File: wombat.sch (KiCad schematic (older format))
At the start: 188 parts, among them J1 Conn_01x01, J2 Conn_01x01, SW1 SW_SPST, SW10 SW_SPST, SW11 SW_SPST, SW12 SW_SPST, SW13 SW_SPST, SW14 SW_SPST, SW15 SW_SPST, SW16 SW_SPST, SW17 SW_SPST, SW18 SW_SPST, SW19 SW_SPST, SW2 SW_SPST, SW20 SW_SPST, SW21 SW_SPST, SW22 SW_SPST, SW23 SW_SPST, SW24 SW_SPST, SW25 SW_SPST, SW26 SW_SPST, SW27 SW_SPST, SW28 SW_SPST, SW29 SW_SPST, SW3 SW_SPST, SW30 SW_SPST, SW31 SW_SPST, SW32 SW_SPST, SW33 SW_SPST, SW34 SW_SPST, SW35 SW_SPST, SW36 SW_SPST, SW37 SW_SPST, SW38 SW_SPST, SW39 SW_SPST, SW4 SW_SPST, SW40 SW_SPST, SW41 SW_SPST, SW42 SW_SPST, SW43 SW_Push, SW44 SW_SPST, SW45 SW_SPST, SW46 SW_SPST, SW47 SW_SPST, SW5 SW_SPST, SW6 SW_SPST, SW7 SW_SPST, SW8 SW_SPST, SW9 SW_SPST, U1 ProMicro

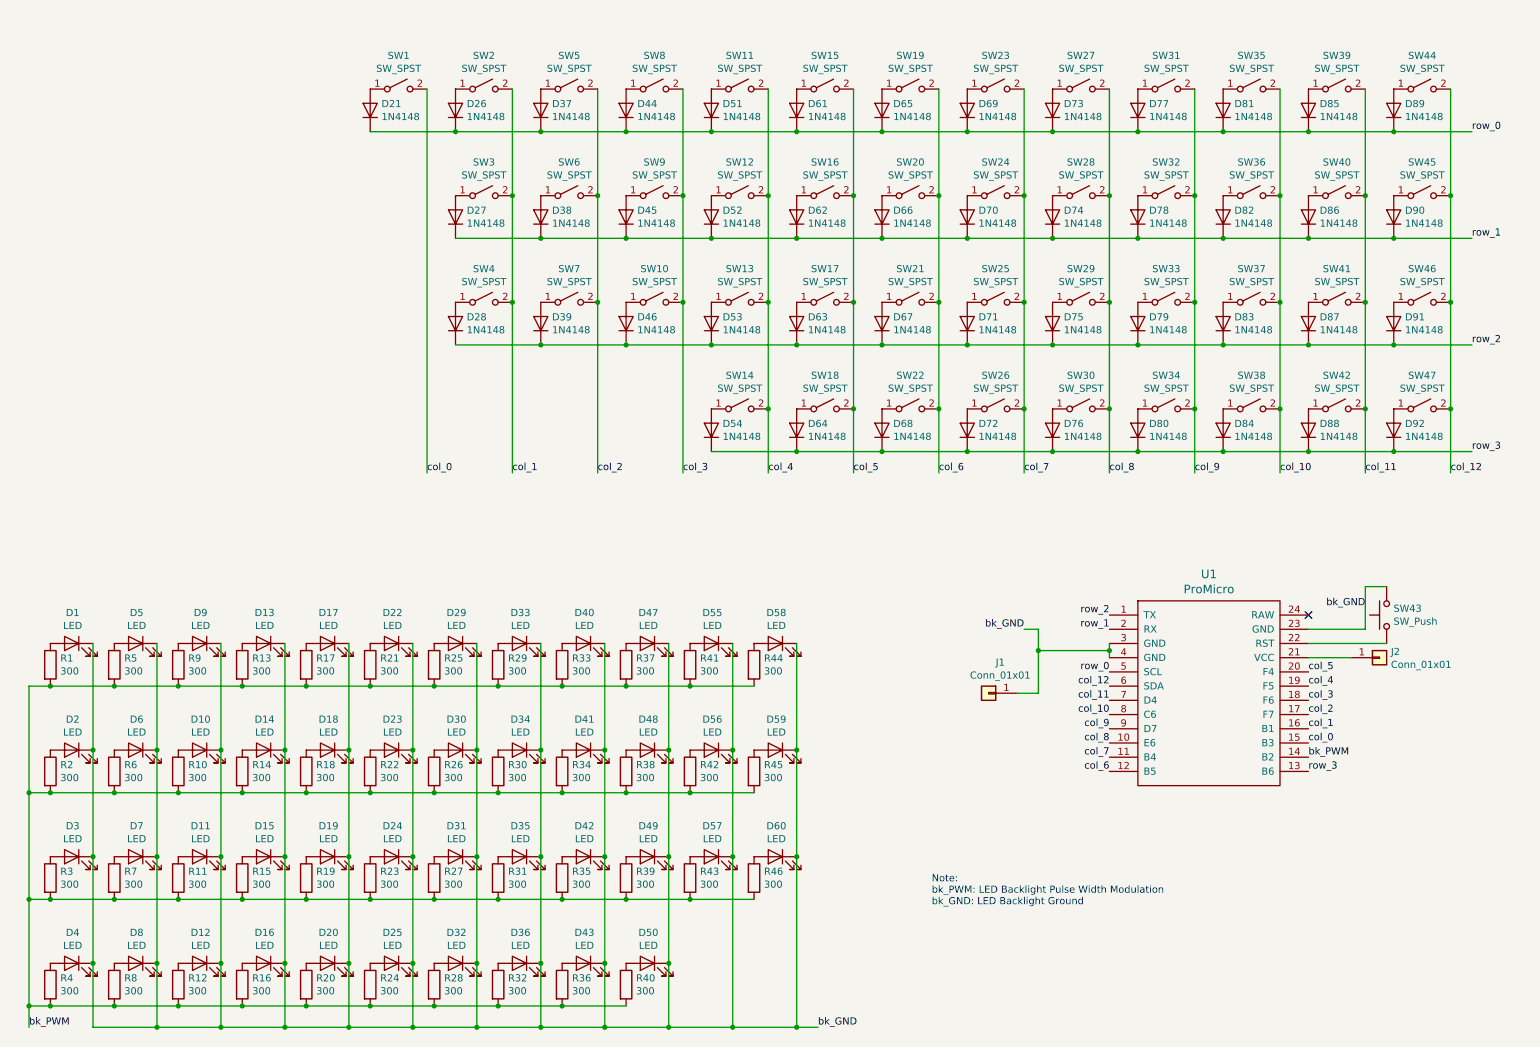
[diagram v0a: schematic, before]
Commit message: annotate components
associate symbols to footprints
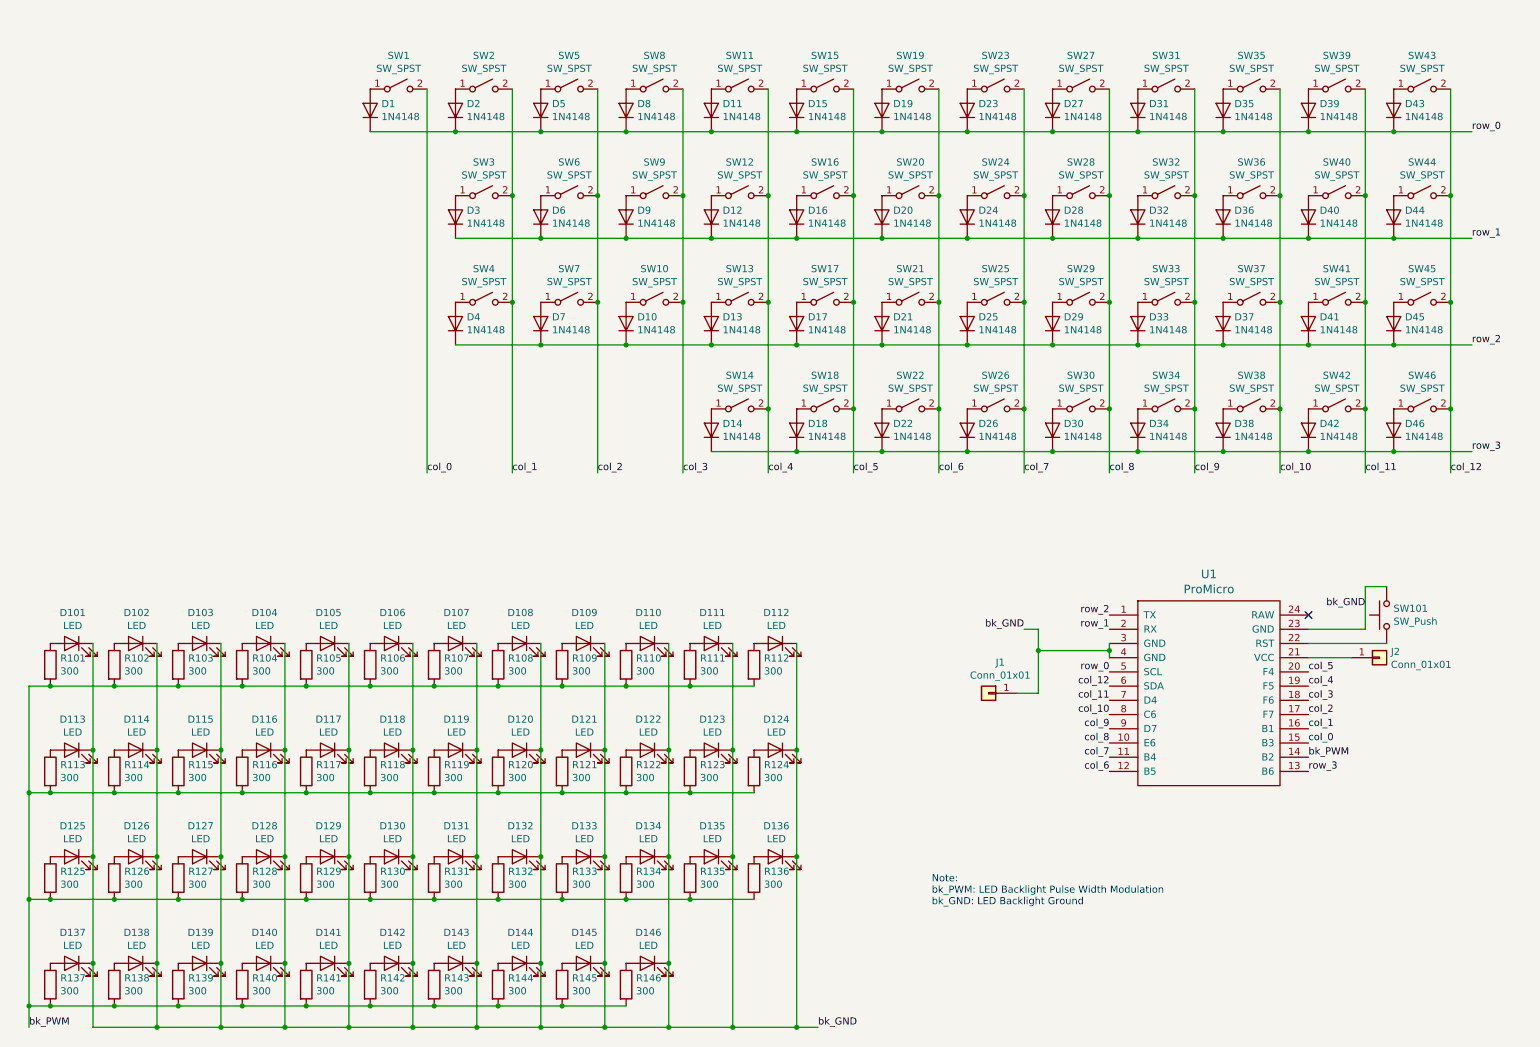
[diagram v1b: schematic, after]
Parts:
- D1: renamed from D21; footprint Diode_THT:D_DO-35_SOD27_P7.62mm_Horizontal -> Diode_SMD:D_0805_2012Metric_Pad1.15x1.40mm_HandSolder
- D10: renamed from D46; footprint Diode_THT:D_DO-35_SOD27_P7.62mm_Horizontal -> Diode_SMD:D_SOD-123
- D101: renamed from D1; footprint (none) -> LED_THT:LED_D2.0mm_W4.8mm_H2.5mm_FlatTop
- D102: renamed from D5; footprint (none) -> LED_THT:LED_D2.0mm_W4.8mm_H2.5mm_FlatTop
- D103: renamed from D9; footprint (none) -> LED_THT:LED_D2.0mm_W4.8mm_H2.5mm_FlatTop
- D104: renamed from D13; footprint (none) -> LED_THT:LED_D2.0mm_W4.8mm_H2.5mm_FlatTop
- D105: renamed from D17; footprint (none) -> LED_THT:LED_D2.0mm_W4.8mm_H2.5mm_FlatTop
- D106: renamed from D22; footprint (none) -> LED_THT:LED_D2.0mm_W4.8mm_H2.5mm_FlatTop
- D107: renamed from D29; footprint (none) -> LED_THT:LED_D2.0mm_W4.8mm_H2.5mm_FlatTop
- D108: renamed from D33; footprint (none) -> LED_THT:LED_D2.0mm_W4.8mm_H2.5mm_FlatTop
- D109: renamed from D40; footprint (none) -> LED_THT:LED_D2.0mm_W4.8mm_H2.5mm_FlatTop
- D11: renamed from D51; footprint Diode_THT:D_DO-35_SOD27_P7.62mm_Horizontal -> Diode_SMD:D_SOD-123
- D110: renamed from D47; footprint (none) -> LED_THT:LED_D2.0mm_W4.8mm_H2.5mm_FlatTop
- D111: renamed from D55; footprint (none) -> LED_THT:LED_D2.0mm_W4.8mm_H2.5mm_FlatTop
- D112: renamed from D58; footprint (none) -> LED_THT:LED_D2.0mm_W4.8mm_H2.5mm_FlatTop
- D113: renamed from D2; footprint (none) -> LED_THT:LED_D2.0mm_W4.8mm_H2.5mm_FlatTop
- D114: renamed from D6; footprint (none) -> LED_THT:LED_D2.0mm_W4.8mm_H2.5mm_FlatTop
- D115: renamed from D10; footprint (none) -> LED_THT:LED_D2.0mm_W4.8mm_H2.5mm_FlatTop
- D116: renamed from D14; footprint (none) -> LED_THT:LED_D2.0mm_W4.8mm_H2.5mm_FlatTop
- D117: renamed from D18; footprint (none) -> LED_THT:LED_D2.0mm_W4.8mm_H2.5mm_FlatTop
- D118: renamed from D23; footprint (none) -> LED_THT:LED_D2.0mm_W4.8mm_H2.5mm_FlatTop
- D119: renamed from D30; footprint (none) -> LED_THT:LED_D2.0mm_W4.8mm_H2.5mm_FlatTop
- D12: renamed from D52; footprint Diode_THT:D_DO-35_SOD27_P7.62mm_Horizontal -> Diode_SMD:D_SOD-123
- D120: renamed from D34; footprint (none) -> LED_THT:LED_D2.0mm_W4.8mm_H2.5mm_FlatTop
- D121: renamed from D41; footprint (none) -> LED_THT:LED_D2.0mm_W4.8mm_H2.5mm_FlatTop
- D122: renamed from D48; footprint (none) -> LED_THT:LED_D2.0mm_W4.8mm_H2.5mm_FlatTop
- D123: renamed from D56; footprint (none) -> LED_THT:LED_D2.0mm_W4.8mm_H2.5mm_FlatTop
- D124: renamed from D59; footprint (none) -> LED_THT:LED_D2.0mm_W4.8mm_H2.5mm_FlatTop
- D125: renamed from D3; footprint (none) -> LED_THT:LED_D2.0mm_W4.8mm_H2.5mm_FlatTop
- D126: renamed from D7; footprint (none) -> LED_THT:LED_D2.0mm_W4.8mm_H2.5mm_FlatTop
- D127: renamed from D11; footprint (none) -> LED_THT:LED_D2.0mm_W4.8mm_H2.5mm_FlatTop
- D128: renamed from D15; footprint (none) -> LED_THT:LED_D2.0mm_W4.8mm_H2.5mm_FlatTop
- D129: renamed from D19; footprint (none) -> LED_THT:LED_D2.0mm_W4.8mm_H2.5mm_FlatTop
- D13: renamed from D53; footprint Diode_THT:D_DO-35_SOD27_P7.62mm_Horizontal -> Diode_SMD:D_SOD-123
- D130: renamed from D24; footprint (none) -> LED_THT:LED_D2.0mm_W4.8mm_H2.5mm_FlatTop
- D131: renamed from D31; footprint (none) -> LED_THT:LED_D2.0mm_W4.8mm_H2.5mm_FlatTop
- D132: renamed from D35; footprint (none) -> LED_THT:LED_D2.0mm_W4.8mm_H2.5mm_FlatTop
- D133: renamed from D42; footprint (none) -> LED_THT:LED_D2.0mm_W4.8mm_H2.5mm_FlatTop
- D134: renamed from D49; footprint (none) -> LED_THT:LED_D2.0mm_W4.8mm_H2.5mm_FlatTop
- D135: renamed from D57; footprint (none) -> LED_THT:LED_D2.0mm_W4.8mm_H2.5mm_FlatTop
- D136: renamed from D60; footprint (none) -> LED_THT:LED_D2.0mm_W4.8mm_H2.5mm_FlatTop
- D137: renamed from D4; footprint (none) -> LED_THT:LED_D2.0mm_W4.8mm_H2.5mm_FlatTop
- D138: renamed from D8; footprint (none) -> LED_THT:LED_D2.0mm_W4.8mm_H2.5mm_FlatTop
- D139: renamed from D12; footprint (none) -> LED_THT:LED_D2.0mm_W4.8mm_H2.5mm_FlatTop
- D14: renamed from D54; footprint Diode_THT:D_DO-35_SOD27_P7.62mm_Horizontal -> Diode_SMD:D_SOD-123
- D140: renamed from D16; footprint (none) -> LED_THT:LED_D2.0mm_W4.8mm_H2.5mm_FlatTop
- D141: renamed from D20; footprint (none) -> LED_THT:LED_D2.0mm_W4.8mm_H2.5mm_FlatTop
- D142: renamed from D25; footprint (none) -> LED_THT:LED_D2.0mm_W4.8mm_H2.5mm_FlatTop
- D143: renamed from D32; footprint (none) -> LED_THT:LED_D2.0mm_W4.8mm_H2.5mm_FlatTop
- D144: renamed from D36; footprint (none) -> LED_THT:LED_D2.0mm_W4.8mm_H2.5mm_FlatTop
- D145: renamed from D43; footprint (none) -> LED_THT:LED_D2.0mm_W4.8mm_H2.5mm_FlatTop
- D146: renamed from D50; footprint (none) -> LED_THT:LED_D2.0mm_W4.8mm_H2.5mm_FlatTop
- D15: renamed from D61; footprint Diode_THT:D_DO-35_SOD27_P7.62mm_Horizontal -> Diode_SMD:D_SOD-123
- D16: renamed from D62; footprint Diode_THT:D_DO-35_SOD27_P7.62mm_Horizontal -> Diode_SMD:D_SOD-123
- D17: renamed from D63; footprint Diode_THT:D_DO-35_SOD27_P7.62mm_Horizontal -> Diode_SMD:D_SOD-123
- D18: renamed from D64; footprint Diode_THT:D_DO-35_SOD27_P7.62mm_Horizontal -> Diode_SMD:D_SOD-123
- D19: renamed from D65; footprint Diode_THT:D_DO-35_SOD27_P7.62mm_Horizontal -> Diode_SMD:D_SOD-123
- D2: renamed from D26; footprint Diode_THT:D_DO-35_SOD27_P7.62mm_Horizontal -> Diode_SMD:D_SOD-123
- D20: renamed from D66; footprint Diode_THT:D_DO-35_SOD27_P7.62mm_Horizontal -> Diode_SMD:D_SOD-123
- D21: renamed from D67; footprint Diode_THT:D_DO-35_SOD27_P7.62mm_Horizontal -> Diode_SMD:D_SOD-123
- D22: renamed from D68; footprint Diode_THT:D_DO-35_SOD27_P7.62mm_Horizontal -> Diode_SMD:D_SOD-123
- D23: renamed from D69; footprint Diode_THT:D_DO-35_SOD27_P7.62mm_Horizontal -> Diode_SMD:D_SOD-123
- D24: renamed from D70; footprint Diode_THT:D_DO-35_SOD27_P7.62mm_Horizontal -> Diode_SMD:D_SOD-123
- D25: renamed from D71; footprint Diode_THT:D_DO-35_SOD27_P7.62mm_Horizontal -> Diode_SMD:D_SOD-123
- D26: renamed from D72; footprint Diode_THT:D_DO-35_SOD27_P7.62mm_Horizontal -> Diode_SMD:D_SOD-123
- D27: renamed from D73; footprint Diode_THT:D_DO-35_SOD27_P7.62mm_Horizontal -> Diode_SMD:D_SOD-123
- D28: renamed from D74; footprint Diode_THT:D_DO-35_SOD27_P7.62mm_Horizontal -> Diode_SMD:D_SOD-123
- D29: renamed from D75; footprint Diode_THT:D_DO-35_SOD27_P7.62mm_Horizontal -> Diode_SMD:D_SOD-123
- D3: renamed from D27; footprint Diode_THT:D_DO-35_SOD27_P7.62mm_Horizontal -> Diode_SMD:D_SOD-123
- D30: renamed from D76; footprint Diode_THT:D_DO-35_SOD27_P7.62mm_Horizontal -> Diode_SMD:D_SOD-123
- D31: renamed from D77; footprint Diode_THT:D_DO-35_SOD27_P7.62mm_Horizontal -> Diode_SMD:D_SOD-123
- D32: renamed from D78; footprint Diode_THT:D_DO-35_SOD27_P7.62mm_Horizontal -> Diode_SMD:D_SOD-123
- D33: renamed from D79; footprint Diode_THT:D_DO-35_SOD27_P7.62mm_Horizontal -> Diode_SMD:D_SOD-123
- D34: renamed from D80; footprint Diode_THT:D_DO-35_SOD27_P7.62mm_Horizontal -> Diode_SMD:D_SOD-123
- D35: renamed from D81; footprint Diode_THT:D_DO-35_SOD27_P7.62mm_Horizontal -> Diode_SMD:D_SOD-123
- D36: renamed from D82; footprint Diode_THT:D_DO-35_SOD27_P7.62mm_Horizontal -> Diode_SMD:D_SOD-123
- D37: renamed from D83; footprint Diode_THT:D_DO-35_SOD27_P7.62mm_Horizontal -> Diode_SMD:D_SOD-123
- D38: renamed from D84; footprint Diode_THT:D_DO-35_SOD27_P7.62mm_Horizontal -> Diode_SMD:D_SOD-123
- D39: renamed from D85; footprint Diode_THT:D_DO-35_SOD27_P7.62mm_Horizontal -> Diode_SMD:D_SOD-123
- D4: renamed from D28; footprint Diode_THT:D_DO-35_SOD27_P7.62mm_Horizontal -> Diode_SMD:D_SOD-123
- D40: renamed from D86; footprint Diode_THT:D_DO-35_SOD27_P7.62mm_Horizontal -> Diode_SMD:D_SOD-123
- D41: renamed from D87; footprint Diode_THT:D_DO-35_SOD27_P7.62mm_Horizontal -> Diode_SMD:D_SOD-123
- D42: renamed from D88; footprint Diode_THT:D_DO-35_SOD27_P7.62mm_Horizontal -> Diode_SMD:D_SOD-123
- D43: renamed from D89; footprint Diode_THT:D_DO-35_SOD27_P7.62mm_Horizontal -> Diode_SMD:D_SOD-123
- D44: renamed from D90; footprint Diode_THT:D_DO-35_SOD27_P7.62mm_Horizontal -> Diode_SMD:D_SOD-123
- D45: renamed from D91; footprint Diode_THT:D_DO-35_SOD27_P7.62mm_Horizontal -> Diode_SMD:D_SOD-123
- D46: renamed from D92; footprint Diode_THT:D_DO-35_SOD27_P7.62mm_Horizontal -> Diode_SMD:D_SOD-123
- D5: renamed from D37; footprint Diode_THT:D_DO-35_SOD27_P7.62mm_Horizontal -> Diode_SMD:D_SOD-123
- D6: renamed from D38; footprint Diode_THT:D_DO-35_SOD27_P7.62mm_Horizontal -> Diode_SMD:D_SOD-123
- D7: renamed from D39; footprint Diode_THT:D_DO-35_SOD27_P7.62mm_Horizontal -> Diode_SMD:D_SOD-123
- D8: renamed from D44; footprint Diode_THT:D_DO-35_SOD27_P7.62mm_Horizontal -> Diode_SMD:D_SOD-123
- D9: renamed from D45; footprint Diode_THT:D_DO-35_SOD27_P7.62mm_Horizontal -> Diode_SMD:D_SOD-123
- J1, J2: footprint (none) -> Connector_Wire:SolderWirePad_1x01_Drill1.5mm
- R101: renamed from R1; footprint (none) -> Resistor_SMD:R_0805_2012Metric_Pad1.15x1.40mm_HandSolder
- R102: renamed from R5; footprint (none) -> Resistor_SMD:R_0805_2012Metric_Pad1.15x1.40mm_HandSolder
- R103: renamed from R9; footprint (none) -> Resistor_SMD:R_0805_2012Metric_Pad1.15x1.40mm_HandSolder
- R104: renamed from R13; footprint (none) -> Resistor_SMD:R_0805_2012Metric_Pad1.15x1.40mm_HandSolder
- R105: renamed from R17; footprint (none) -> Resistor_SMD:R_0805_2012Metric_Pad1.15x1.40mm_HandSolder
- R106: renamed from R21; footprint (none) -> Resistor_SMD:R_0805_2012Metric_Pad1.15x1.40mm_HandSolder
- R107: renamed from R25; footprint (none) -> Resistor_SMD:R_0805_2012Metric_Pad1.15x1.40mm_HandSolder
- R108: renamed from R29; footprint (none) -> Resistor_SMD:R_0805_2012Metric_Pad1.15x1.40mm_HandSolder
- R109: renamed from R33; footprint (none) -> Resistor_SMD:R_0805_2012Metric_Pad1.15x1.40mm_HandSolder
- R110: renamed from R37; footprint (none) -> Resistor_SMD:R_0805_2012Metric_Pad1.15x1.40mm_HandSolder
- R111: renamed from R41; footprint (none) -> Resistor_SMD:R_0805_2012Metric_Pad1.15x1.40mm_HandSolder
- R112: renamed from R44; footprint (none) -> Resistor_SMD:R_0805_2012Metric_Pad1.15x1.40mm_HandSolder
- R113: renamed from R2; footprint (none) -> Resistor_SMD:R_0805_2012Metric_Pad1.15x1.40mm_HandSolder
- R114: renamed from R6; footprint (none) -> Resistor_SMD:R_0805_2012Metric_Pad1.15x1.40mm_HandSolder
- R115: renamed from R10; footprint (none) -> Resistor_SMD:R_0805_2012Metric_Pad1.15x1.40mm_HandSolder
- R116: renamed from R14; footprint (none) -> Resistor_SMD:R_0805_2012Metric_Pad1.15x1.40mm_HandSolder
- R117: renamed from R18; footprint (none) -> Resistor_SMD:R_0805_2012Metric_Pad1.15x1.40mm_HandSolder
- R118: renamed from R22; footprint (none) -> Resistor_SMD:R_0805_2012Metric_Pad1.15x1.40mm_HandSolder
- R119: renamed from R26; footprint (none) -> Resistor_SMD:R_0805_2012Metric_Pad1.15x1.40mm_HandSolder
- R120: renamed from R30; footprint (none) -> Resistor_SMD:R_0805_2012Metric_Pad1.15x1.40mm_HandSolder
- R121: renamed from R34; footprint (none) -> Resistor_SMD:R_0805_2012Metric_Pad1.15x1.40mm_HandSolder
- R122: renamed from R38; footprint (none) -> Resistor_SMD:R_0805_2012Metric_Pad1.15x1.40mm_HandSolder
- R123: renamed from R42; footprint (none) -> Resistor_SMD:R_0805_2012Metric_Pad1.15x1.40mm_HandSolder
- R124: renamed from R45; footprint (none) -> Resistor_SMD:R_0805_2012Metric_Pad1.15x1.40mm_HandSolder
- R125: renamed from R3; footprint (none) -> Resistor_SMD:R_0805_2012Metric_Pad1.15x1.40mm_HandSolder
- R126: renamed from R7; footprint (none) -> Resistor_SMD:R_0805_2012Metric_Pad1.15x1.40mm_HandSolder
- R127: renamed from R11; footprint (none) -> Resistor_SMD:R_0805_2012Metric_Pad1.15x1.40mm_HandSolder
- R128: renamed from R15; footprint (none) -> Resistor_SMD:R_0805_2012Metric_Pad1.15x1.40mm_HandSolder
- R129: renamed from R19; footprint (none) -> Resistor_SMD:R_0805_2012Metric_Pad1.15x1.40mm_HandSolder
- R130: renamed from R23; footprint (none) -> Resistor_SMD:R_0805_2012Metric_Pad1.15x1.40mm_HandSolder
- R131: renamed from R27; footprint (none) -> Resistor_SMD:R_0805_2012Metric_Pad1.15x1.40mm_HandSolder
- R132: renamed from R31; footprint (none) -> Resistor_SMD:R_0805_2012Metric_Pad1.15x1.40mm_HandSolder
- R133: renamed from R35; footprint (none) -> Resistor_SMD:R_0805_2012Metric_Pad1.15x1.40mm_HandSolder
- R134: renamed from R39; footprint (none) -> Resistor_SMD:R_0805_2012Metric_Pad1.15x1.40mm_HandSolder
- R135: renamed from R43; footprint (none) -> Resistor_SMD:R_0805_2012Metric_Pad1.15x1.40mm_HandSolder
- R136: renamed from R46; footprint (none) -> Resistor_SMD:R_0805_2012Metric_Pad1.15x1.40mm_HandSolder
- R137: renamed from R4; footprint (none) -> Resistor_SMD:R_0805_2012Metric_Pad1.15x1.40mm_HandSolder
- R138: renamed from R8; footprint (none) -> Resistor_SMD:R_0805_2012Metric_Pad1.15x1.40mm_HandSolder
- R139: renamed from R12; footprint (none) -> Resistor_SMD:R_0805_2012Metric_Pad1.15x1.40mm_HandSolder
- R140: renamed from R16; footprint (none) -> Resistor_SMD:R_0805_2012Metric_Pad1.15x1.40mm_HandSolder
- R141: renamed from R20; footprint (none) -> Resistor_SMD:R_0805_2012Metric_Pad1.15x1.40mm_HandSolder
- R142: renamed from R24; footprint (none) -> Resistor_SMD:R_0805_2012Metric_Pad1.15x1.40mm_HandSolder
- R143: renamed from R28; footprint (none) -> Resistor_SMD:R_0805_2012Metric_Pad1.15x1.40mm_HandSolder
- R144: renamed from R32; footprint (none) -> Resistor_SMD:R_0805_2012Metric_Pad1.15x1.40mm_HandSolder
- R145: renamed from R36; footprint (none) -> Resistor_SMD:R_0805_2012Metric_Pad1.15x1.40mm_HandSolder
- R146: renamed from R40; footprint (none) -> Resistor_SMD:R_0805_2012Metric_Pad1.15x1.40mm_HandSolder
- SW1, SW10, SW11, SW12, SW13, SW14, SW15, SW16, SW17, SW19, SW2, SW20, SW21, SW23, SW24, SW25, SW27, SW28, SW29, SW31, SW32, SW33, SW35, SW36, SW37, SW39, SW40, SW41, SW5, SW6, SW7, SW8, SW9: footprint (none) -> keebs-github:Mx_Alps_100
- SW101: renamed from SW43; footprint (none) -> Button_Switch_SMD:SW_Push_1P1T_NO_6x6mm_H9.5mm
- SW18, SW22, SW26, SW38, SW4, SW42: footprint (none) -> keebs-github:Mx_Alps_125
- SW3: footprint (none) -> keebs-github:Mx_Alps_175
- SW30, SW34: footprint (none) -> keebs-github:Mx_Alps_225
- SW43: renamed from SW44; footprint (none) -> keebs-github:Mx_Alps_100
- SW44: renamed from SW45; footprint (none) -> keebs-github:Mx_Alps_125
- SW45: renamed from SW46; footprint (none) -> keebs-github:Mx_Alps_175
- SW46: renamed from SW47; footprint (none) -> keebs-github:Mx_Alps_125
- U1: footprint (none) -> keebs-github:Pro_Micro

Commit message: layout board
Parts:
- D101, D102, D103, D104, D105, D106, D107, D108, D109, D110, D111, D112, D113, D114, D115, D116, D117, D118, D119, D120, D121, D122, D123, D124, D125, D126, D127, D128, D129, D130, D131, D132, D133, D134, D135, D136, D137, D138, D139, D140, D141, D142, D143, D144, D145, D146: footprint LED_THT:LED_D2.0mm_W4.8mm_H2.5mm_FlatTop -> keebs-github:LED_D2.0mm_W4.8mm_H2.5mm_FlatTop_Reverse_Polarity
- J1, J2: footprint Connector_Wire:SolderWirePad_1x01_Drill1.5mm -> Connector_Wire:SolderWirePad_1x01_Drill0.8mm
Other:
- moved on the sheet: D113, D114, D115, D116, D117, D118, D119, D120, D121, D122, D123, D124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

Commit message: change orientation of mc
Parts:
- SW101: footprint Button_Switch_SMD:SW_Push_1P1T_NO_6x6mm_H9.5mm -> Button_Switch_SMD:SW_SPST_EVQP0
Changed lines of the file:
@@
 F 0 "SW101" V 10246 4702 50  0000 R CNN
 F 1 "SW_Push" V 10155 4702 50  0000 R CNN
-F 2 "Button_Switch_SMD:SW_Push_1P1T_NO_6x6mm_H9.5mm" H 10200 4950 50  0001 C CNN
+F 2 "Button_Switch_SMD:SW_SPST_EVQP0" H 10200 4950 50  0001 C CNN
 F 3 "~" H 10200 4950 50  0001 C CNN
 	1    10200 4750

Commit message: route traces
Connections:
- net bk_GND: no longer SW101.2, U1.23 (GND)
- new net: SW101.2, U1.23 (GND)
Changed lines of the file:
@@
 Text Label 7650 4850 2    50   ~ 0
-bk_GND
-Text Label 10050 4700 2    50   ~ 0
 bk_GND
 Text Label 8250 5650 2    50   ~ 0
